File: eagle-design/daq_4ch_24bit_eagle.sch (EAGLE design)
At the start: 177 parts, among them J1 B6252HB-NPP3G-50, J2 B6252HB-NPP3G-50, J3 USB, J4 B6252HB-NPP3G-50, J5 B6252HB-NPP3G-50, J6 B6252HB-NPP3G-50, J7 B6252HB-NPP3G-50, U1 TS5A3359DCU, U10 74LVC1G3157, U11 ADS122U04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

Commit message: Fixes to schematic and library, begin placement and routing
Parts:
- LED1: value (none) -> GREEN
- R30, R31: value (none) -> 10k
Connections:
- net N$27 renamed USBGND
- net N$28 renamed VUSB
- net N$32 renamed USBD_P
- net N$33 renamed USBD_N
- net USB-D+ renamed USB-D_P
- net USB-D- renamed USB-D_N
- removed net N$16: D15.A, RN1B.2
- removed net N$17: D16.A, RN1C.2
- removed net N$18: D17.A, RN1D.2
- removed net N$19: D13.A, RN1A.2
- net ADC_CH2: no longer U10.A
- net ADC_CH3: now also U10.A
- net CH0_SW1: now also D13.A, RN1A.2
- net CH0_SW2: now also D15.A, RN1B.2
- net CH1_SW1: now also D16.A, RN1C.2
- net CH1_SW2: now also D17.A, RN1D.2
- net GND: now also TP4.TP, Y1.2; no longer TP2.TP, Y1.3
- net N$40: now also Y1.1; no longer Y1.2
- net N$41: now also Y1.3; no longer Y1.1
- net N$48: now also TP1.TP; no longer TP3.TP
- net N$71: now also TP2.TP; no longer TP4.TP
- net VAA: now also U8B.V+
- net VBUS: now also TP3.TP; no longer TP1.TP
- net VSS: now also U8B.GND
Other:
- moved on the sheet: TP1, TP2, TP3, TP4, Y1

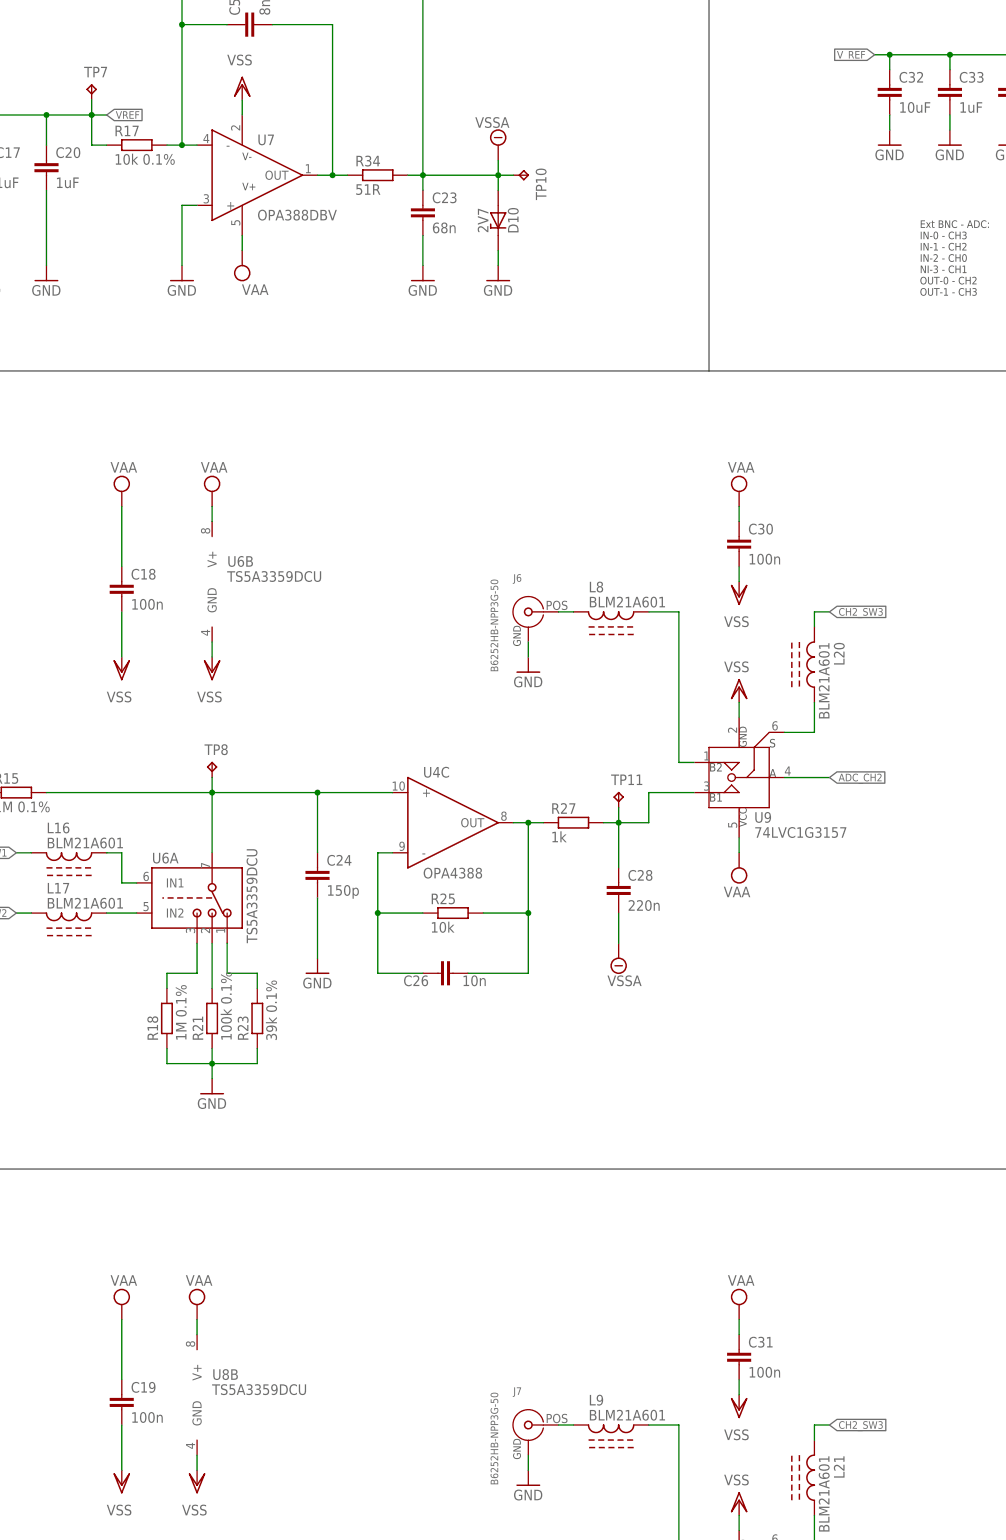
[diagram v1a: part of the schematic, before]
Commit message: Fix on schematic, placement and routing done, needs impendance calculation, first iteration - could be improved
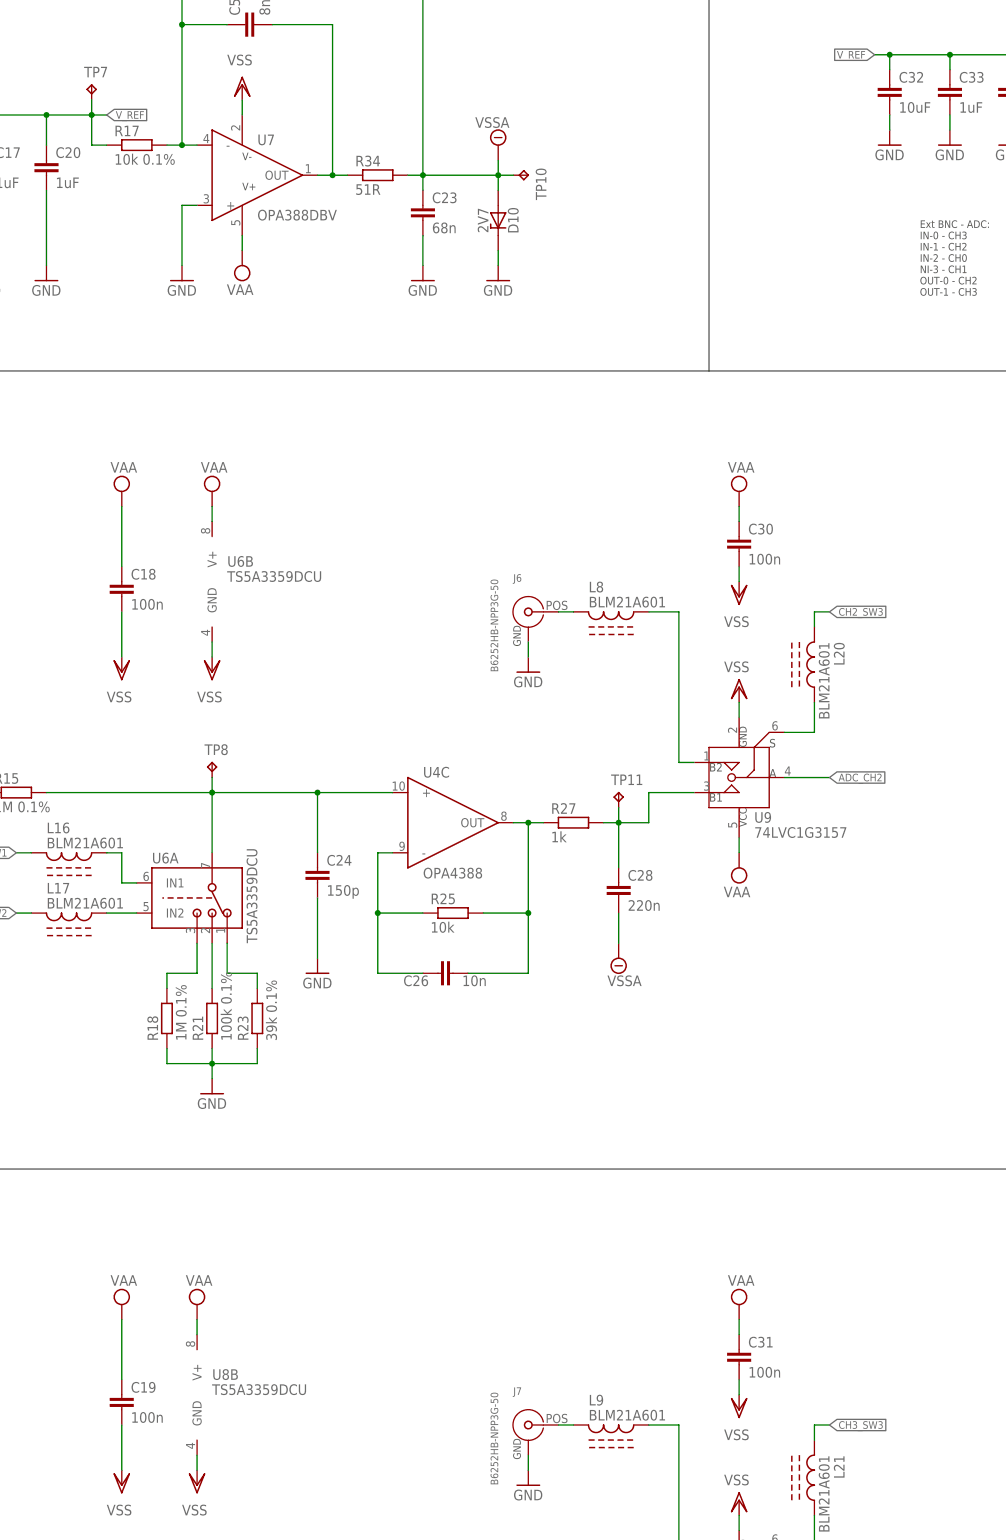
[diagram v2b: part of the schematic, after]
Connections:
- removed net VREF: C20.1, R17.1, TP7.TP, U5.VOUT
- net CH2_SW3: no longer L21.P$1
- net CH3_SW3: now also L21.P$1
- net VAA: now also U7.V+
- net VDD: no longer U7.V+
- net V_REF: now also C20.1, R17.1, TP7.TP, U5.VOUT
